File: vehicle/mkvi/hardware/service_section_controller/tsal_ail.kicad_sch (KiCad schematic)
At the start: 28 parts, among them J601 NanoFit_2, Q601 SSM3K333R, Q602 SSM3K333R, Q603 SSM3K333R, U601 MCP6001, U602 CPC1025NTR, U603 BU4S11G2-TR

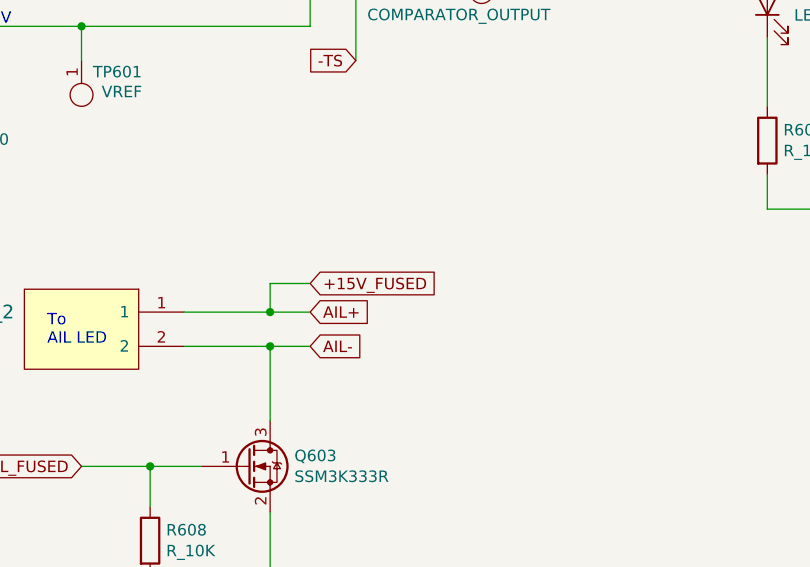
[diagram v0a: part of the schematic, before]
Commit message: Updated ss controller schematic
update schematic based on Dasha's comments
- didn't fix IMD NAND latch symbol
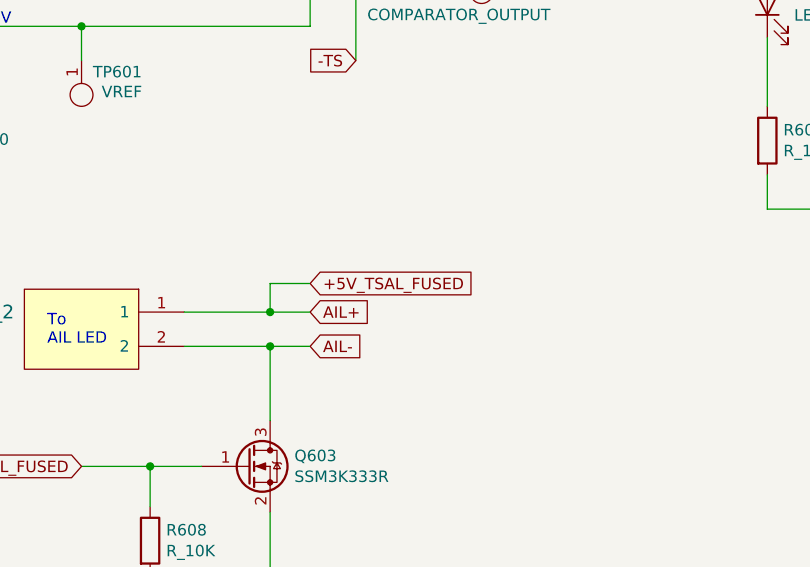
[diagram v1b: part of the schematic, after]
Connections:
- net +15V_FUSED renamed +5V_TSAL_FUSED
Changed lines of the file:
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@@
     )
   )
-  (global_label "+15V_FUSED" (shape input) (at 96.52 144.145 0) (fields_autoplaced)
+  (global_label "+5V_TSAL_FUSED" (shape input) (at 96.52 144.145 0) (fields_autoplaced)
     (effects (font (size 1.27 1.27)) (justify left))
-    (property "Intersheet References" "${INTERSHEET_REFS}" (id 0) (at 0 0 0)
-      (effects (font (size 1.27 1.27)) hide)
+    (property "Intersheet References" "${INTERSHEET_REFS}" (id 0) (at 114.9913 144.0656 0)
+      (effects (font (size 1.27 1.27)) (justify left) hide)
     )
   )

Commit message: Revert "Updated ss controller schematic"
This reverts commit e92fea9276160b711cab1a1c4b2a2633d6ea79b5.
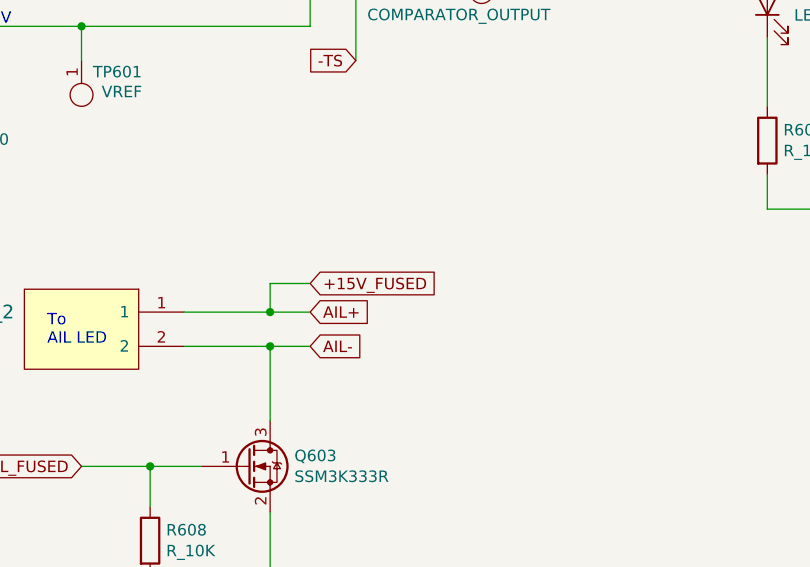
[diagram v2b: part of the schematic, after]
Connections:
- net +5V_TSAL_FUSED renamed +15V_FUSED
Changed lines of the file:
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@@
     )
   )
-  (global_label "+5V_TSAL_FUSED" (shape input) (at 96.52 144.145 0) (fields_autoplaced)
+  (global_label "+15V_FUSED" (shape input) (at 96.52 144.145 0) (fields_autoplaced)
     (effects (font (size 1.27 1.27)) (justify left))
-    (property "Intersheet References" "${INTERSHEET_REFS}" (id 0) (at 114.9913 144.0656 0)
-      (effects (font (size 1.27 1.27)) (justify left) hide)
+    (property "Intersheet References" "${INTERSHEET_REFS}" (id 0) (at 0 0 0)
+      (effects (font (size 1.27 1.27)) hide)
     )
   )

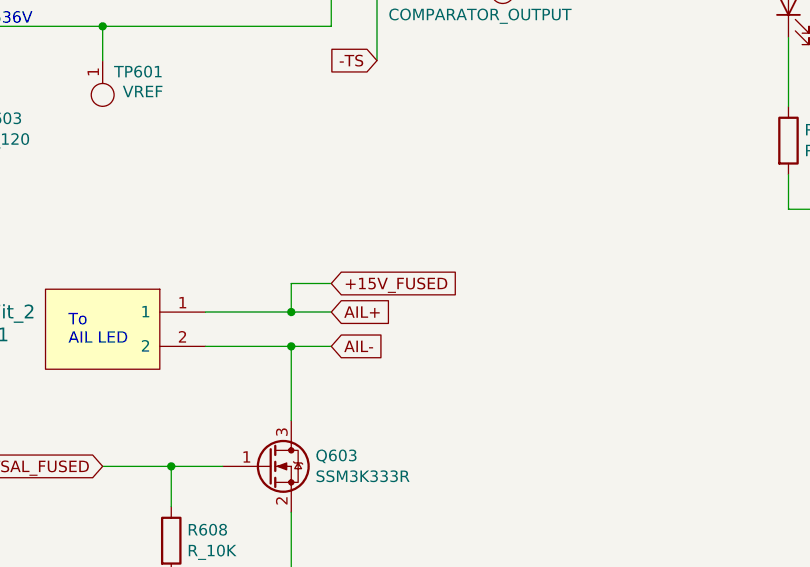
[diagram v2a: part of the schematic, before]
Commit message: schematic finished
made edits to schematic according to comments :)
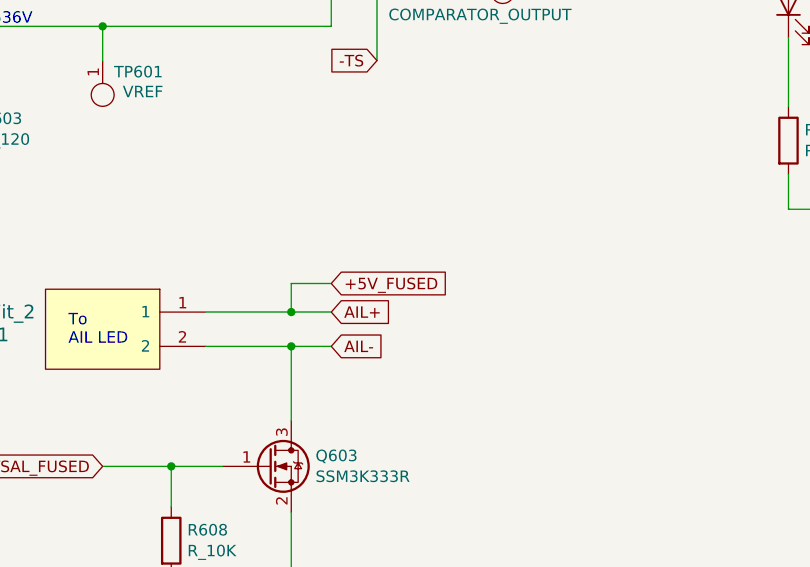
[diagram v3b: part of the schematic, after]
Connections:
- net +15V_FUSED renamed +5V_FUSED
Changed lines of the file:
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@@
     )
   )
-  (global_label "+15V_FUSED" (shape input) (at 96.52 144.145 0) (fields_autoplaced)
+  (global_label "+5V_FUSED" (shape input) (at 96.52 144.145 0) (fields_autoplaced)
     (effects (font (size 1.27 1.27)) (justify left))
-    (property "Intersheet References" "${INTERSHEET_REFS}" (id 0) (at 0 0 0)
-      (effects (font (size 1.27 1.27)) hide)
+    (property "Intersheet References" "${INTERSHEET_REFS}" (id 0) (at 109.7299 144.0656 0)
+      (effects (font (size 1.27 1.27)) (justify left) hide)
     )
   )
